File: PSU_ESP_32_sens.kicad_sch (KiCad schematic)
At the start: 21 parts, among them J3 USB_C_Receptacle_USB2.0_16P, U5 HT7533-1, U6 USBLC6-2SC6, U7 TLV62569DBV

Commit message: additional comment
additional comment
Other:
- note added: "PSU design is heavily inspired by Phils Lab design *"
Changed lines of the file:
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@@
+		)
+	)
+	(text "PSU design is heavily inspired by Phils Lab design *"
+		(exclude_from_sim no)
+		(at 257.81 16.256 0)
+		(effects
+			(font
+				(size 1.27 1.27)
+			)
 		)
 	)

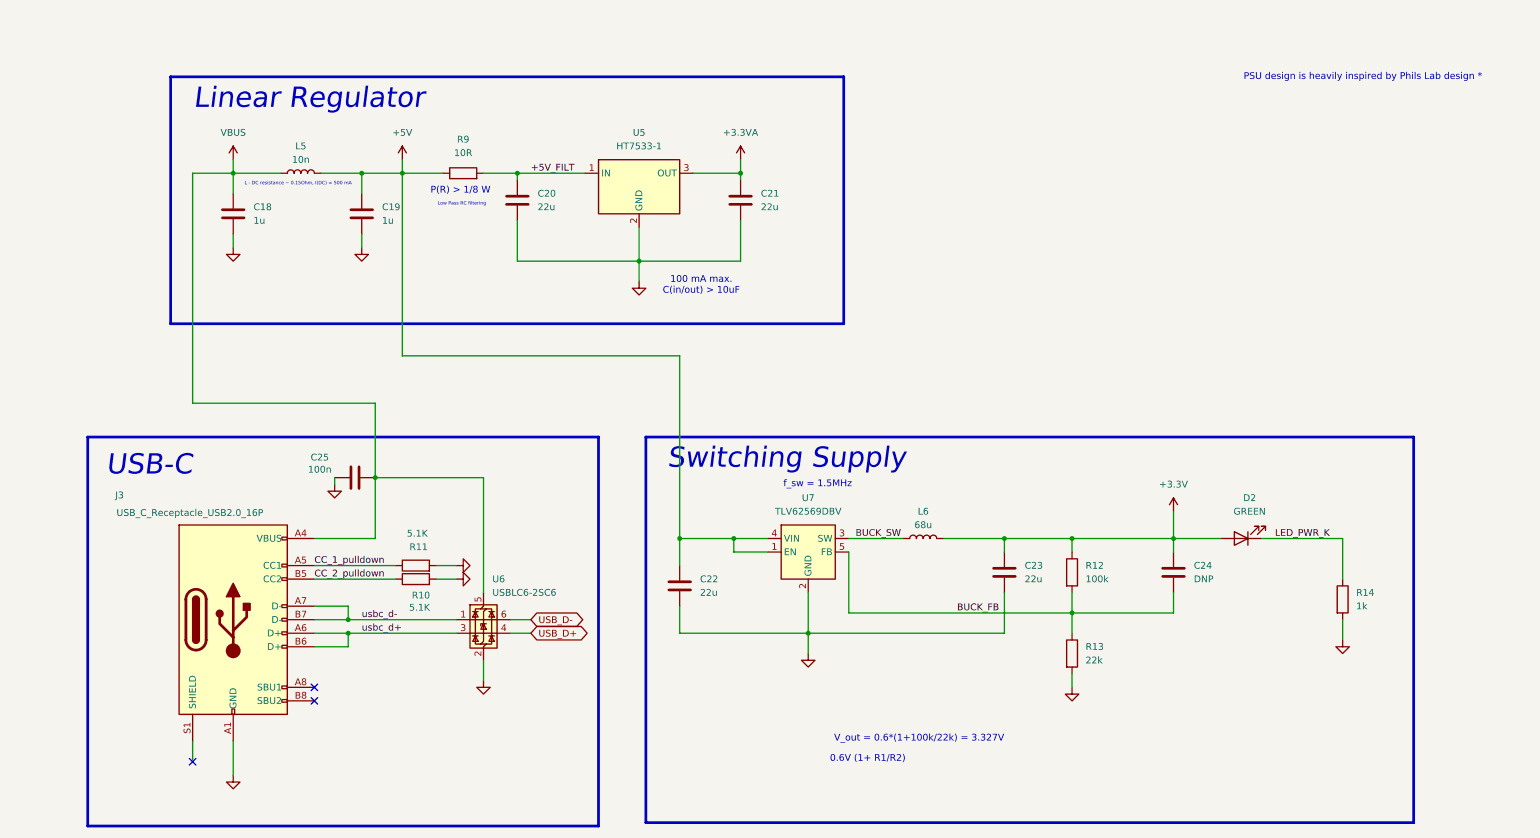
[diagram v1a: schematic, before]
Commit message: placement done
placement done, routing left
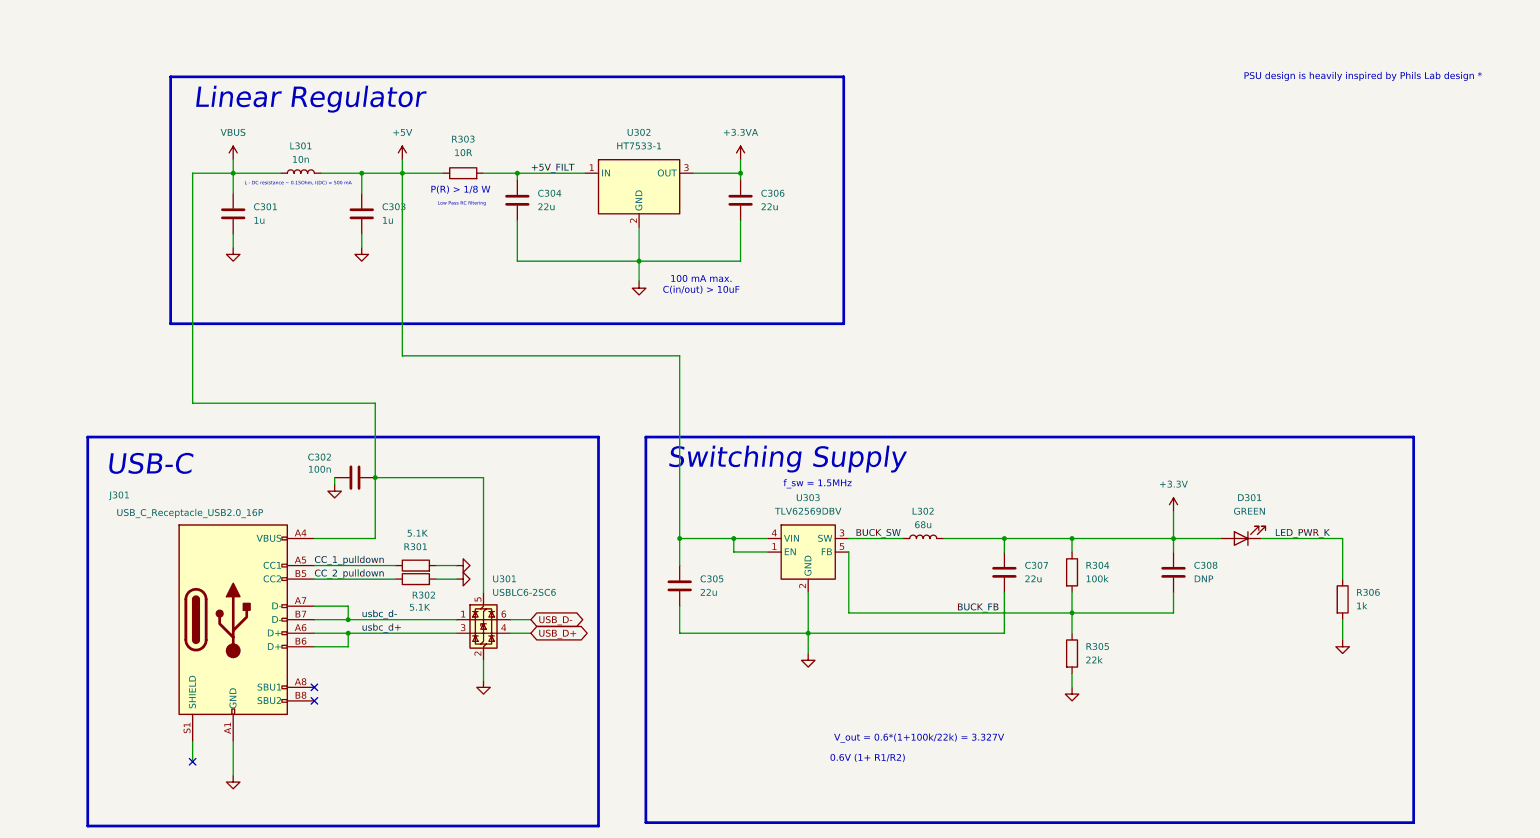
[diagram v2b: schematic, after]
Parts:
- renumbered C18 to C301, C25 to C302, C19 to C303, C20 to C304, C22 to C305, C21 to C306, C23 to C307, C24 to C308, D2 to D301, J3 to J301, L5 to L301, L6 to L302, R11 to R301, R10 to R302, R9 to R303, R12 to R304, R13 to R305, R14 to R306, U6 to U301, U5 to U302, U7 to U303

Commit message: changes
changes made
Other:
- note added: "PSU design is inspired by Phils Lab design *"
- note removed: "PSU design is heavily inspired by Phils Lab design *"
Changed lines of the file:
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@@
 		)
 	)
-	(text "PSU design is heavily inspired by Phils Lab design *"
+	(text "PSU design is inspired by Phils Lab design *"
 		(exclude_from_sim no)
-		(at 257.81 16.256 0)
+		(at 30.48 5.334 0)
 		(effects
 			(font
